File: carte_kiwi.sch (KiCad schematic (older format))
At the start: 40 parts, among them IC1 MCP2562, P1 CONN_01X05, P2 CONN_01X03, P3 CONN_01X05, P4 CONN_01X03, P5 Serial Wire, P6 CAN_conn, P7 CONN_01X03, P8 CONN_01X03, P9 CAN_conn, SW1 SW_PUSH_SMALL_H, U1 LD1117S50TR, U2 LD1117S33TR, U3 STM32F303K8

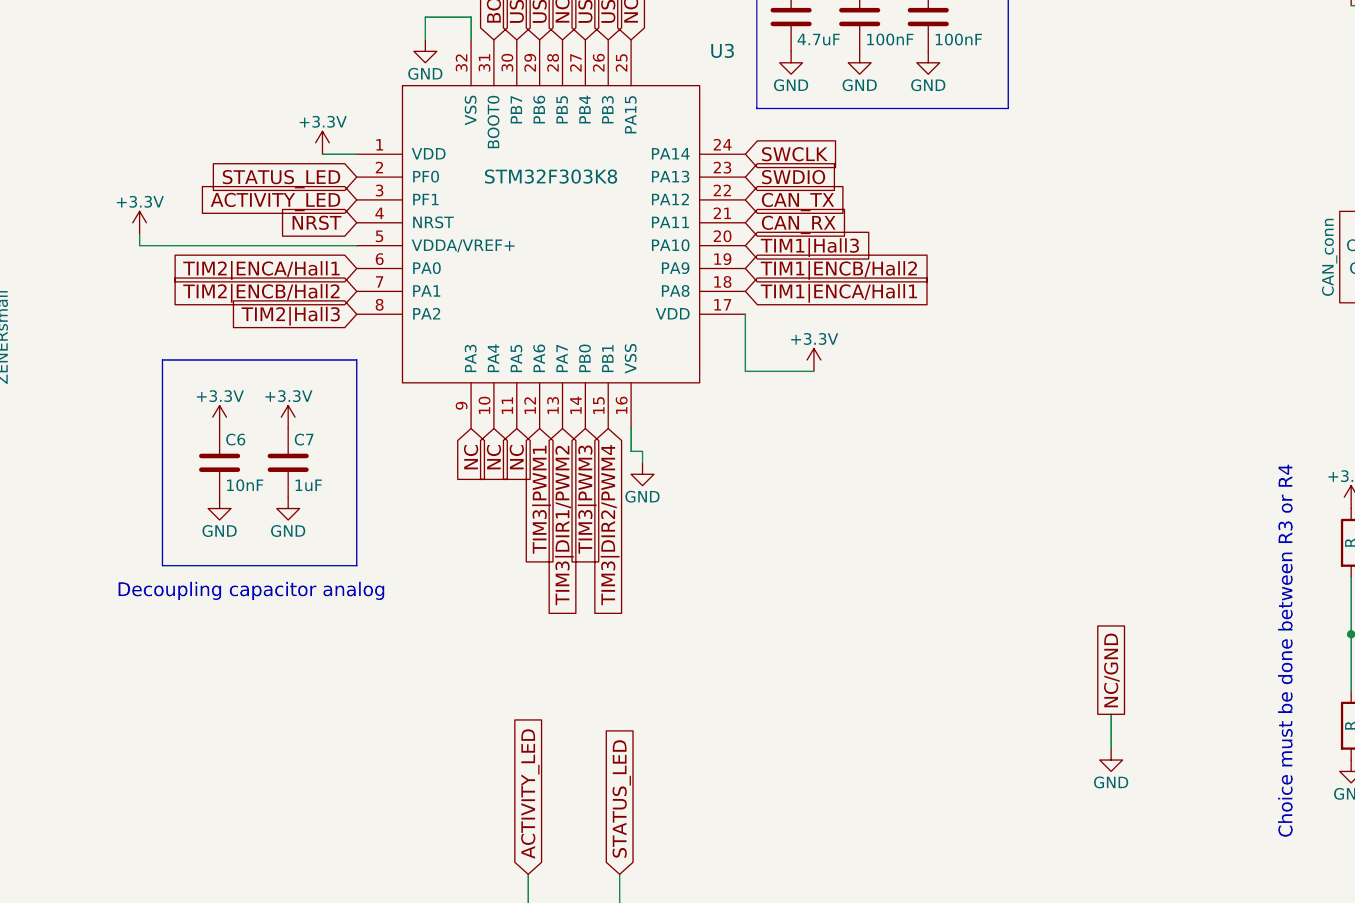
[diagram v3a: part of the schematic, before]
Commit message: routage terminé mais à nettoyer
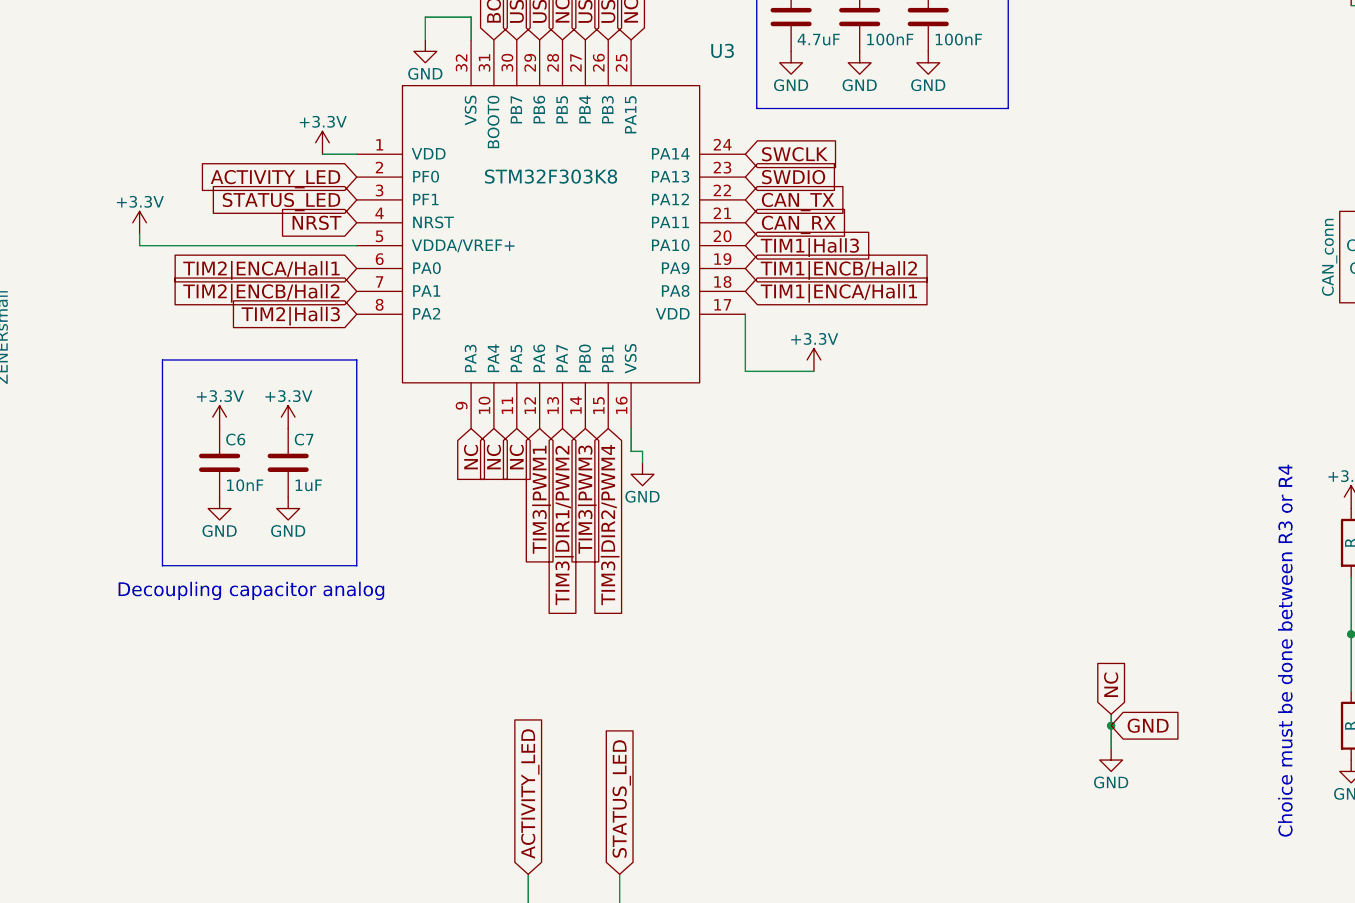
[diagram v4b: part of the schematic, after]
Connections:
- net NC is gone; now on net GND: U3.10 (PA4), U3.11 (PA5), U3.25 (PA15), U3.28 (PB5), U3.9 (PA3)
- net ACTIVITY_LED: now also U3.2 (PF0); no longer U3.3 (PF1)
- net STATUS_LED: now also U3.3 (PF1); no longer U3.2 (PF0)
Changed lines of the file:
@@
 Text GLabel 10100 900  2    60   Input ~ 0
 USART1_RX/SDA
-Text GLabel 4650 3400 0    60   Input ~ 0
+Text GLabel 4650 3500 0    60   Input ~ 0
 STATUS_LED
 Text GLabel 5800 6450 1    60   Input ~ 0
@@
 Wire Wire Line
 	5400 6600 5400 6450
-Text GLabel 4650 3500 0    60   Input ~ 0
+Text GLabel 4650 3400 0    60   Input ~ 0
 ACTIVITY_LED
 Wire Wire Line
@@
 Text GLabel 5350 4500 3    60   Input ~ 0
 NC
-Text GLabel 7950 5750 1    60   UnSpc ~ 0
-NC/GND
 $Comp
 L GND #PWR043
@@
 Text Notes 6350 2200 0    60   ~ 0
 Decoupling capacitor digital
+Text GLabel 7950 5750 1    60   Input ~ 0
+NC
+Text GLabel 7950 5800 2    60   Input ~ 0
+GND
+Connection ~ 7950 5800
 $EndSCHEMATC

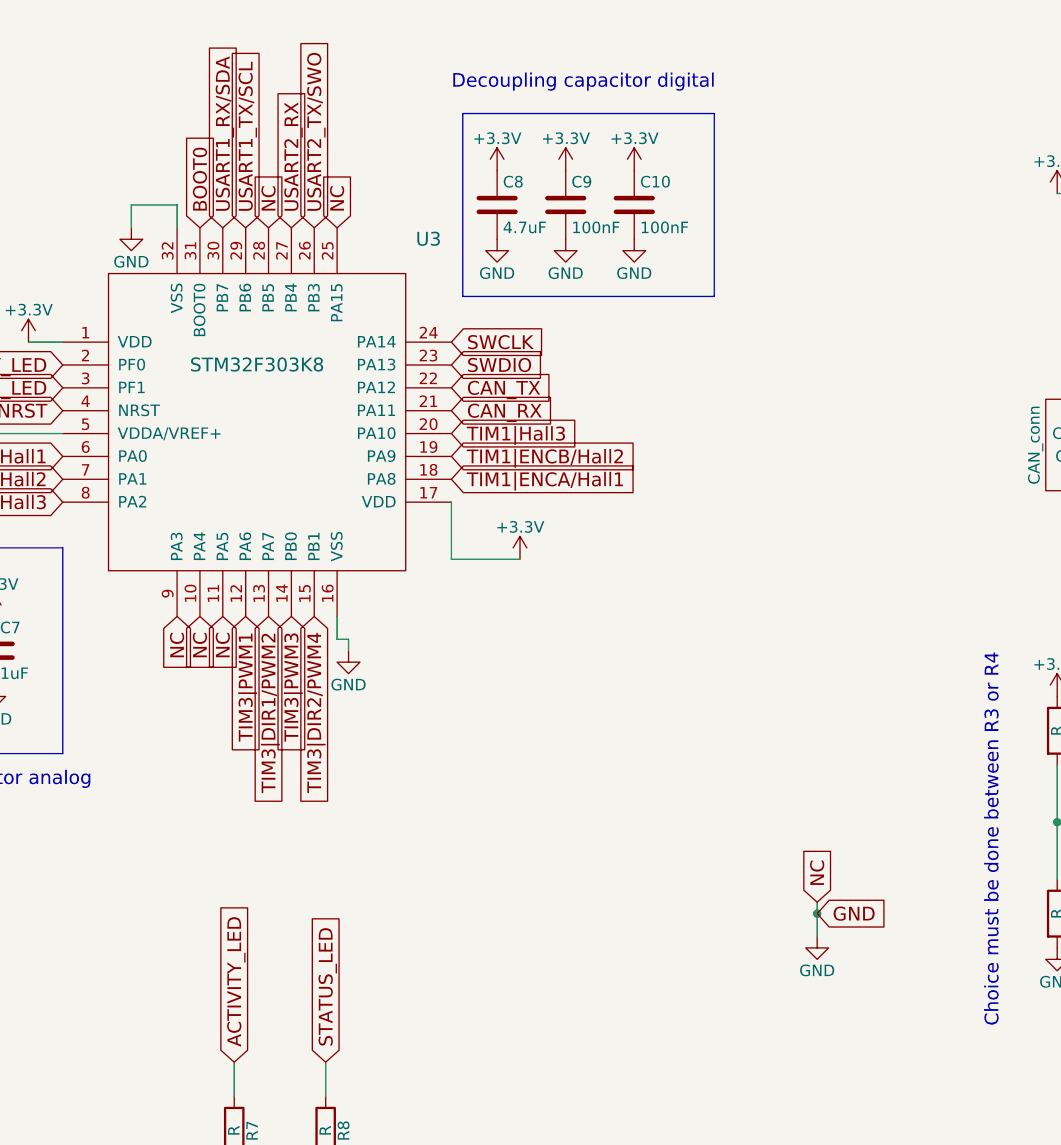
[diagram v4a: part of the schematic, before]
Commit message: retire les connexions à GND des pins non utilisées
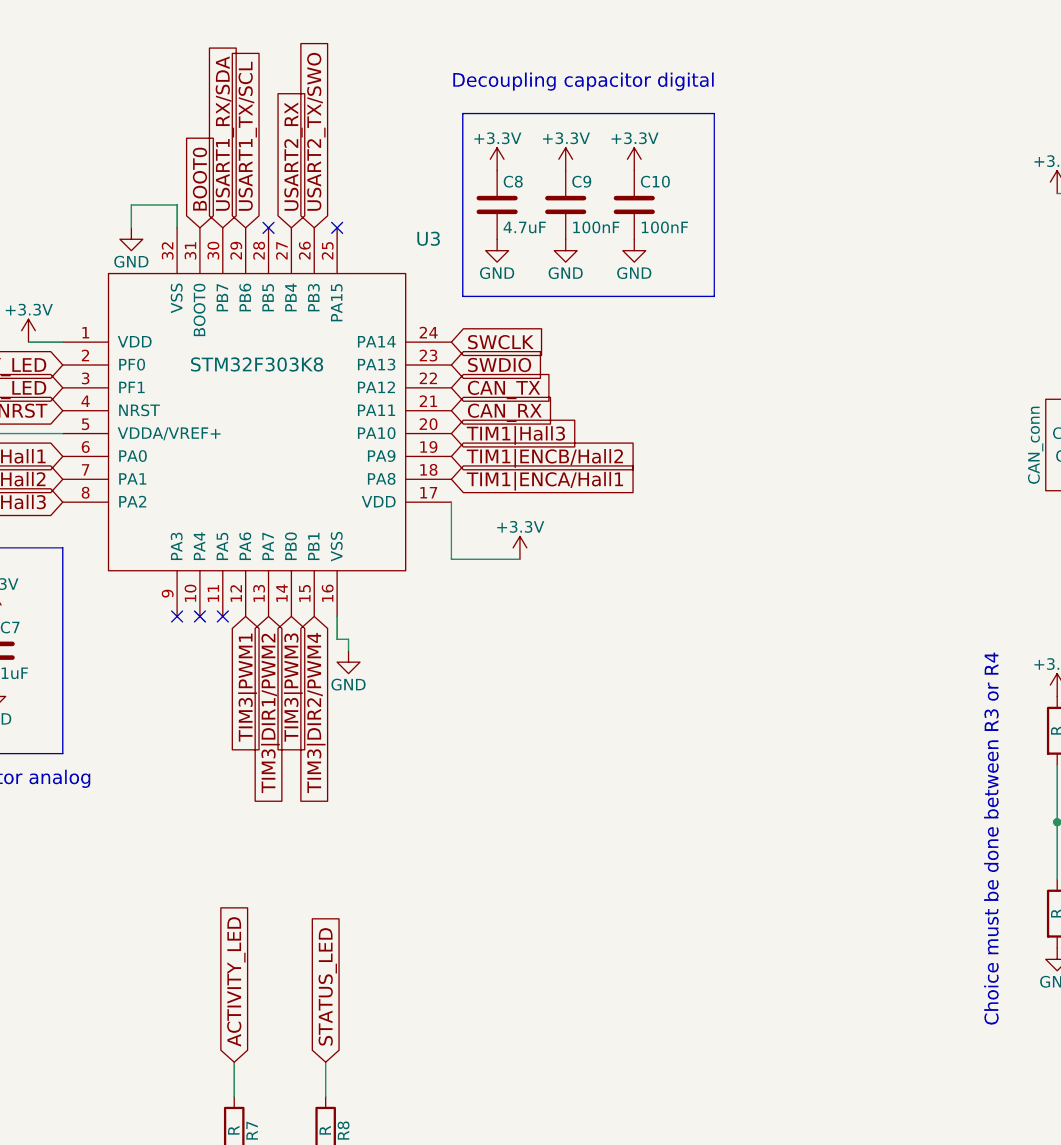
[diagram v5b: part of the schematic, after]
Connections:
- net GND: no longer U3.10 (PA4), U3.11 (PA5), U3.25 (PA15), U3.28 (PB5), U3.9 (PA3)
- no-connect marks 0 -> 5
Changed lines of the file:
@@
 Text Notes 3900 1550 0    60   ~ 0
 Allow choice between 3.3V or 5V
-Text GLabel 5550 2800 1    60   Input ~ 0
-NC
-Text GLabel 5850 2800 1    60   Input ~ 0
-NC
-Text GLabel 5150 4500 3    60   Input ~ 0
-NC
-Text GLabel 5250 4500 3    60   Input ~ 0
-NC
-Text GLabel 5350 4500 3    60   Input ~ 0
-NC
-$Comp
-L GND #PWR043
-U 1 1 589D2058
-P 7950 5900
-F 0 "#PWR043" H 7950 5650 50  0001 C CNN
-F 1 "GND" H 7950 5750 50  0000 C CNN
-F 2 "" H 7950 5900 50  0000 C CNN
-F 3 "" H 7950 5900 50  0000 C CNN
-	1    7950 5900
-	1    0    0    -1
-$EndComp
-Wire Wire Line
-	7950 5900 7950 5750
 Text GLabel 5350 2800 1    60   Input ~ 0
 USART1_RX/SDA
@@
 $EndComp
 $Comp
-L GND #PWR044
+L GND #PWR043
 U 1 1 589E6CEE
 P 10200 1600
-F 0 "#PWR044" H 10200 1350 50  0001 C CNN
+F 0 "#PWR043" H 10200 1350 50  0001 C CNN
 F 1 "GND" H 10200 1450 50  0000 C CNN
 F 2 "" H 10200 1600 50  0000 C CNN
@@
 	10100 1550 10200 1550
 $Comp
-L GND #PWR045
+L GND #PWR044
 U 1 1 589E6DA5
 P 10200 1050
-F 0 "#PWR045" H 10200 800 50  0001 C CNN
+F 0 "#PWR044" H 10200 800 50  0001 C CNN
 F 1 "GND" H 10200 900 50  0000 C CNN
 F 2 "" H 10200 1050 50  0000 C CNN
@@
 $EndComp
 $Comp
-L +3.3V #PWR046
+L +3.3V #PWR045
 U 1 1 589E9230
 P 6550 2550
-F 0 "#PWR046" H 6550 2400 50  0001 C CNN
+F 0 "#PWR045" H 6550 2400 50  0001 C CNN
 F 1 "+3.3V" H 6550 2690 50  0000 C CNN
 F 2 "" H 6550 2550 50  0000 C CNN
@@
 $EndComp
 $Comp
-L +3.3V #PWR047
+L +3.3V #PWR046
 U 1 1 589E92B4
 P 6850 2550
-F 0 "#PWR047" H 6850 2400 50  0001 C CNN
+F 0 "#PWR046" H 6850 2400 50  0001 C CNN
 F 1 "+3.3V" H 6850 2690 50  0000 C CNN
 F 2 "" H 6850 2550 50  0000 C CNN
@@
 $EndComp
 $Comp
-L +3.3V #PWR048
+L +3.3V #PWR047
 U 1 1 589E9357
 P 7150 2550
-F 0 "#PWR048" H 7150 2400 50  0001 C CNN
+F 0 "#PWR047" H 7150 2400 50  0001 C CNN
 F 1 "+3.3V" H 7150 2690 50  0000 C CNN
 F 2 "" H 7150 2550 50  0000 C CNN
@@
 $EndComp
 $Comp
-L GND #PWR049
+L GND #PWR048
 U 1 1 589E93B0
 P 6550 2850
-F 0 "#PWR049" H 6550 2600 50  0001 C CNN
+F 0 "#PWR048" H 6550 2600 50  0001 C CNN
 F 1 "GND" H 6550 2700 50  0000 C CNN
 F 2 "" H 6550 2850 50  0000 C CNN
@@
 $EndComp
 $Comp
-L GND #PWR050
+L GND #PWR049
 U 1 1 589E9434
 P 6850 2850
-F 0 "#PWR050" H 6850 2600 50  0001 C CNN
+F 0 "#PWR049" H 6850 2600 50  0001 C CNN
 F 1 "GND" H 6850 2700 50  0000 C CNN
 F 2 "" H 6850 2850 50  0000 C CNN
@@
 $EndComp
 $Comp
-L GND #PWR051
+L GND #PWR050
 U 1 1 589E94B1
 P 7150 2850
-F 0 "#PWR051" H 7150 2600 50  0001 C CNN
+F 0 "#PWR050" H 7150 2600 50  0001 C CNN
 F 1 "GND" H 7150 2700 50  0000 C CNN
 F 2 "" H 7150 2850 50  0000 C CNN
@@
 $EndComp
 $Comp
-L +3.3V #PWR052
+L +3.3V #PWR051
 U 1 1 589E96D4
 P 4050 4500
-F 0 "#PWR052" H 4050 4350 50  0001 C CNN
+F 0 "#PWR051" H 4050 4350 50  0001 C CNN
 F 1 "+3.3V" H 4050 4640 50  0000 C CNN
 F 2 "" H 4050 4500 50  0000 C CNN
@@
 $EndComp
 $Comp
-L +3.3V #PWR053
+L +3.3V #PWR052
 U 1 1 589E96DA
 P 4350 4500
-F 0 "#PWR053" H 4350 4350 50  0001 C CNN
+F 0 "#PWR052" H 4350 4350 50  0001 C CNN
 F 1 "+3.3V" H 4350 4640 50  0000 C CNN
 F 2 "" H 4350 4500 50  0000 C CNN
@@
 $EndComp
 $Comp
-L GND #PWR054
+L GND #PWR053
 U 1 1 589E96E0
 P 4050 4800
-F 0 "#PWR054" H 4050 4550 50  0001 C CNN
+F 0 "#PWR053" H 4050 4550 50  0001 C CNN
 F 1 "GND" H 4050 4650 50  0000 C CNN
 F 2 "" H 4050 4800 50  0000 C CNN
@@
 $EndComp
 $Comp
-L GND #PWR055
+L GND #PWR054
 U 1 1 589E96E6
 P 4350 4800
-F 0 "#PWR055" H 4350 4550 50  0001 C CNN
+F 0 "#PWR054" H 4350 4550 50  0001 C CNN
 F 1 "GND" H 4350 4650 50  0000 C CNN
 F 2 "" H 4350 4800 50  0000 C CNN
@@
 Text Notes 6350 2200 0    60   ~ 0
 Decoupling capacitor digital
-Text GLabel 7950 5750 1    60   Input ~ 0
-NC
-Text GLabel 7950 5800 2    60   Input ~ 0
-GND
-Connection ~ 7950 5800
+NoConn ~ 5850 2800
+NoConn ~ 5550 2800
+NoConn ~ 5150 4500
+NoConn ~ 5250 4500
+NoConn ~ 5350 4500
 $EndSCHEMATC
